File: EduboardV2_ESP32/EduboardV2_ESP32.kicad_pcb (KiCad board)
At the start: 2 copper layers, 2 parts, among them U1 ESP32-WROOM-E, U2 FT2232HL

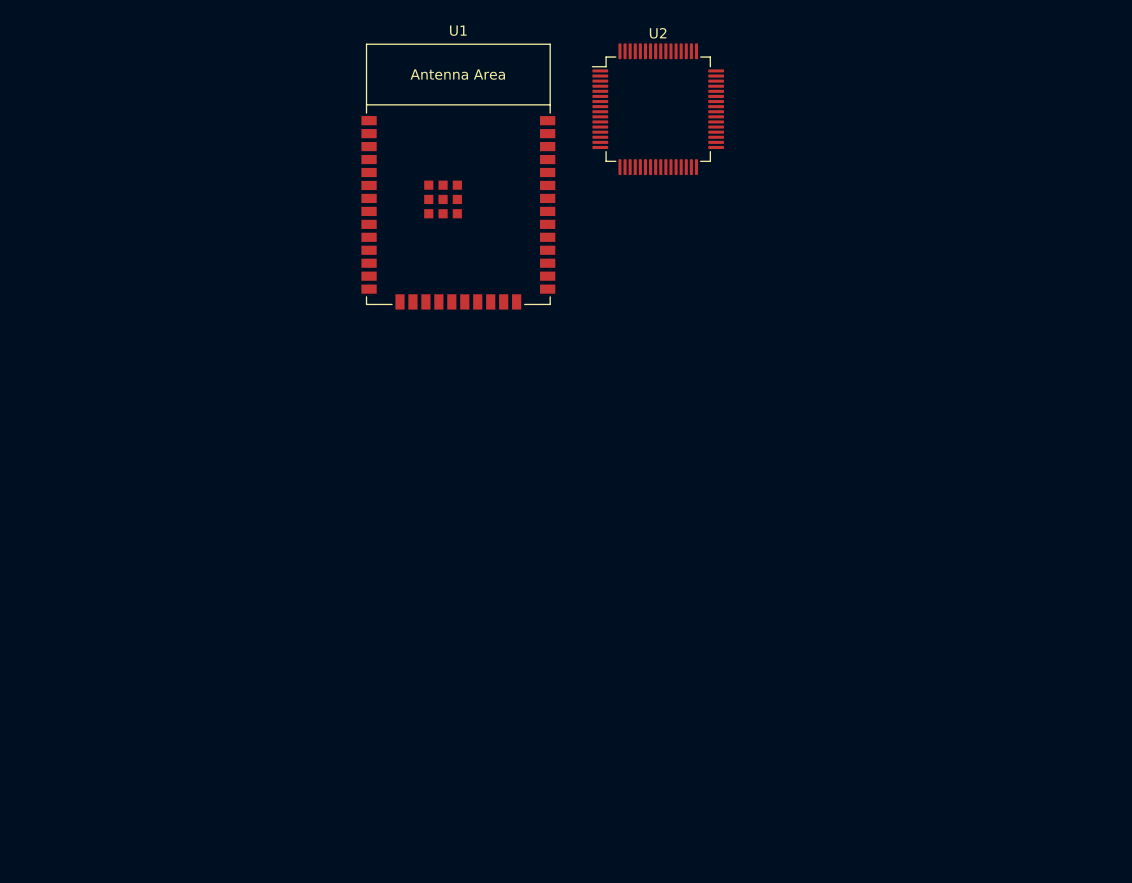
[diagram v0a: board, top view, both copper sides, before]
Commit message: finalize ft2232 design, prepare esp pins, work on mpcie pinout
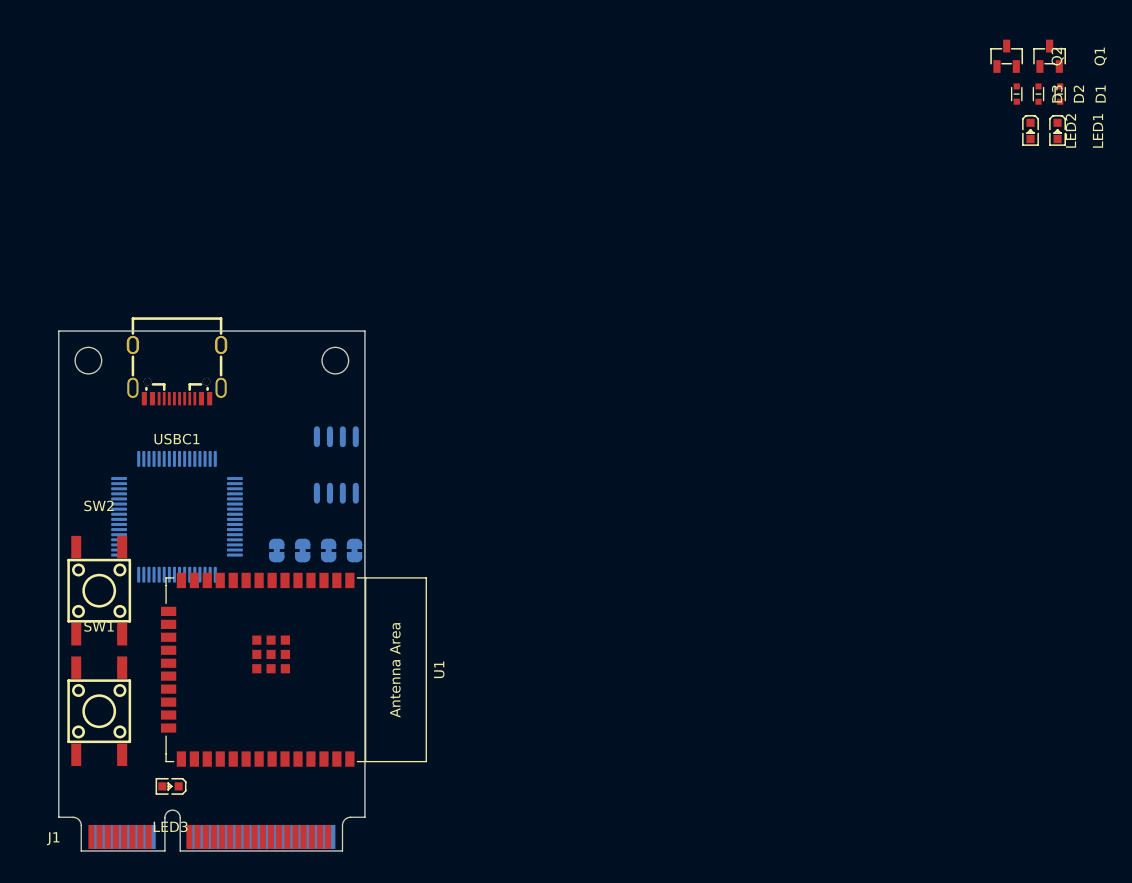
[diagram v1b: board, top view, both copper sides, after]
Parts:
- added D1: LESD5D5.0CT1G, JLCPCB:SOD-523_L1.2-W0.8-LS1.6-BI, F.Cu at (202.4, 82.1)
- added D2: LESD5D5.0CT1G, JLCPCB:SOD-523_L1.2-W0.8-LS1.6-BI, F.Cu at (200.2, 82.1)
- added D3: LESD5D5.0CT1G, JLCPCB:SOD-523_L1.2-W0.8-LS1.6-BI, F.Cu at (198.1, 82.1)
- added J1: Conn_02x26_Odd_Even, mpcie:mini-PCIe_F1_Full, F.Cu at (115.4, 156.3)
- added JP1: SolderJumper_2_Bridged, Jumper:SolderJumper-2_P1.3mm_Bridged_RoundedPad1.0x1.5mm, B.Cu at (133.2, 126.9)
- added JP2: SolderJumper_2_Bridged, Jumper:SolderJumper-2_P1.3mm_Bridged_RoundedPad1.0x1.5mm, B.Cu at (130.7, 126.9)
- added JP3: SolderJumper_2_Bridged, Jumper:SolderJumper-2_P1.3mm_Bridged_RoundedPad1.0x1.5mm, B.Cu at (128.1, 126.9)
- added JP4: SolderJumper_2_Bridged, Jumper:SolderJumper-2_P1.3mm_Bridged_RoundedPad1.0x1.5mm, B.Cu at (125.6, 126.9)
- added LED1: 19-217/BHC-ZL1M2RY/3T, JLCPCB:LED0603-RD, F.Cu at (202.1, 85.8)
- added LED2: 19-217/BHC-ZL1M2RY/3T, JLCPCB:LED0603-RD, F.Cu at (199.5, 85.8)
- added LED3: 19-217/BHC-ZL1M2RY/3T, JLCPCB:LED0603-RD, F.Cu at (115.2, 150.0)
- added Q1: S8050_C139514, JLCPCB:SOT-23-3_L2.9-W1.3-P1.90-LS2.4-BR, F.Cu at (201.3, 78.4)
- added Q2: S8050_C139514, JLCPCB:SOT-23-3_L2.9-W1.3-P1.90-LS2.4-BR, F.Cu at (197.1, 78.4)
- added SW1: K2-1102SP-C4SC-04, JLCPCB:KEY-SMD_4P-L6.0-W6.0-P4.50-LS9.5-BL, F.Cu at (108.2, 142.6)
- added SW2: K2-1102SP-C4SC-04, JLCPCB:KEY-SMD_4P-L6.0-W6.0-P4.50-LS9.5-BL, F.Cu at (108.2, 130.8)
- added U3: M93C46-WMN6TP, JLCPCB:SOIC-8_L4.9-W3.9-P1.27-LS6.0-BL, B.Cu at (131.4, 118.5)
- added USBC1: USB3.1C16PFSMT, JLCPCB:USB-C-SMD_TYPE-C-USB-17, F.Cu at (115.8, 109.4)
- U2: moved to B.Cu
- moved U2 61.8 mm to (115.8, 123.6), turned to -90 degrees
- moved U1 50.0 mm to (125.8, 138.6), turned to -90 degrees
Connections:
- U1 pad 1: Net-(U1-GND-Pad1) -> GND
- U1 pad 13: unconnected-(U1-MTMS/GPIO14/ADC2_CH6-Pad13) -> ESP_TMS
- U1 pad 14: unconnected-(U1-MTDI/GPIO12/ADC2_CH5-Pad14) -> ESP_TDI
- U1 pad 15: Net-(U1-GND-Pad1) -> GND
- U1 pad 16: unconnected-(U1-MTCK/GPIO13/ADC2_CH4-Pad16) -> ESP_TCK
- U1 pad 2: unconnected-(U1-3V3-Pad2) -> +3V3
- U1 pad 23: unconnected-(U1-MTDO/GPIO15/ADC2_CH3-Pad23) -> ESP_TDO
- U1 pad 25: unconnected-(U1-GPIO0/BOOT/ADC2_CH1-Pad25) -> ESP_IO0
- U1 pad 3: unconnected-(U1-EN/CHIP_PU-Pad3) -> ESP_EN
- U1 pad 34: unconnected-(U1-U0RXD/GPIO3-Pad34) -> ESP_RXD
- U1 pad 35: unconnected-(U1-U0TXD/GPIO1-Pad35) -> ESP_TXD
- U1 pad 38: Net-(U1-GND-Pad1) -> GND
- U1 pad 39: unconnected-(U1-GND_THERMAL-Pad39) -> GND
- U2 pad 12: unconnected-(U2-VCORE-Pad12) -> +1V8
- U2 pad 14: unconnected-(U2-~{RESET}-Pad14) -> Net-(U2-~{RESET})
- U2 pad 16: unconnected-(U2-ADBUS0-Pad16) -> FT_TCK
- U2 pad 17: unconnected-(U2-ADBUS1-Pad17) -> FT_TDI
- U2 pad 18: unconnected-(U2-ADBUS2-Pad18) -> FT_TDO
- U2 pad 19: unconnected-(U2-ADBUS3-Pad19) -> FT_TMS
- U2 pad 20: unconnected-(U2-VCCIO-Pad20) -> +3V3
- U2 pad 31: unconnected-(U2-VCCIO-Pad31) -> +3V3
- U2 pad 36: unconnected-(U2-~{SUSPEND}-Pad36) -> nSUSPEND
- U2 pad 37: unconnected-(U2-VCORE-Pad37) -> +1V8
- U2 pad 38: unconnected-(U2-BDBUS0-Pad38) -> FT_TXD
- U2 pad 39: unconnected-(U2-BDBUS1-Pad39) -> FT_RXD
- U2 pad 4: unconnected-(U2-VPHY-Pad4) -> Net-(U2-VPHY)
- U2 pad 40: unconnected-(U2-BDBUS2-Pad40) -> FT_nRTS
- U2 pad 42: unconnected-(U2-VCCIO-Pad42) -> +3V3
- U2 pad 43: unconnected-(U2-BDBUS4-Pad43) -> FT_nDTR
- U2 pad 49: unconnected-(U2-VREGOUT-Pad49) -> +1V8
- U2 pad 50: unconnected-(U2-VREGIN-Pad50) -> +3V3
- U2 pad 54: unconnected-(U2-BCBUS3-Pad54) -> Net-(LED1-C)
- U2 pad 55: unconnected-(U2-BCBUS4-Pad55) -> Net-(LED2-C)
- U2 pad 56: unconnected-(U2-VCCIO-Pad56) -> +3V3
- U2 pad 59: unconnected-(U2-BCBUS7-Pad59) -> nPWRSAV
- U2 pad 6: unconnected-(U2-REF-Pad6) -> Net-(U2-REF)
- U2 pad 60: unconnected-(U2-~{PWREN}-Pad60) -> nPWREN
- U2 pad 61: unconnected-(U2-EEDATA-Pad61) -> Net-(U2-EEDATA)
- U2 pad 62: unconnected-(U2-EECLK-Pad62) -> Net-(U2-EECLK)
- U2 pad 63: unconnected-(U2-EECS-Pad63) -> Net-(U2-EECS)
- U2 pad 64: unconnected-(U2-VCORE-Pad64) -> +1V8
- U2 pad 7: unconnected-(U2-DM-Pad7) -> D-
- U2 pad 8: unconnected-(U2-DP-Pad8) -> D+
- U2 pad 9: unconnected-(U2-VPLL-Pad9) -> Net-(U2-VPLL)
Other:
- board outline added: 30 x 51 mm

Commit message: all parts placed. descision about usb-debug line to be made...
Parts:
- added C1: 12p, Capacitor_SMD:C_0603_1608Metric, B.Cu at (109.7, 113.5)
- added C10: 100n, Capacitor_SMD:C_0603_1608Metric, F.Cu at (117.1, 120.8)
- added C11: 100n, Capacitor_SMD:C_0603_1608Metric, F.Cu at (112.3, 121.5)
- added C12: 100n, Capacitor_SMD:C_0603_1608Metric, B.Cu at (107.7, 126.2)
- added C13: 100n, Capacitor_SMD:C_0603_1608Metric, F.Cu at (112.6, 126.0)
- added C14: 100n, Capacitor_SMD:C_0603_1608Metric, F.Cu at (121.7, 122.8)
- added C15: 100n, Capacitor_SMD:C_0603_1608Metric, F.Cu at (121.7, 125.9)
- added C16: 100n, Capacitor_SMD:C_0603_1608Metric, F.Cu at (115.8, 127.5)
- added C17: 100n, Capacitor_SMD:C_0603_1608Metric, F.Cu at (128.5, 126.7)
- added C18: 100n, Capacitor_SMD:C_0603_1608Metric, B.Cu at (107.7, 136.4)
- added C19: 100n, Capacitor_SMD:C_0603_1608Metric, F.Cu at (132.3, 127.5)
- added C2: 12p, Capacitor_SMD:C_0603_1608Metric, B.Cu at (109.7, 117.1)
- added C20: 1u, Capacitor_SMD:C_0603_1608Metric, F.Cu at (132.3, 125.9)
- added C21: 1u, Capacitor_SMD:C_0603_1608Metric, B.Cu at (122.2, 143.0)
- added C22: 100n, Capacitor_SMD:C_0603_1608Metric, B.Cu at (122.2, 144.5)
- added C23: 100n, Capacitor_SMD:C_0603_1608Metric, B.Cu at (117.9, 148.7)
- added C24: 100n, Capacitor_SMD:C_0603_1608Metric, B.Cu at (126.5, 147.3)
- added C3: 100n, Capacitor_SMD:C_0603_1608Metric, B.Cu at (127.5, 121.8)
- added C4: 4u7, Capacitor_SMD:C_0805_2012Metric, B.Cu at (118.5, 131.4)
- added C5: 4u7, Capacitor_SMD:C_0805_2012Metric, B.Cu at (114.2, 131.3)
- added C6: 4u7, Capacitor_SMD:C_0805_2012Metric, B.Cu at (114.4, 114.3)
- added C7: 4u7, Capacitor_SMD:C_0805_2012Metric, B.Cu at (118.1, 114.3)
- added C8: 100n, Capacitor_SMD:C_0603_1608Metric, B.Cu at (117.9, 116.1)
- added C9: 100n, Capacitor_SMD:C_0603_1608Metric, B.Cu at (114.4, 116.1)
- added FB1: FerriteBead_Small, Inductor_SMD:L_0805_2012Metric, B.Cu at (117.2, 111.5)
- added FB2: FerriteBead_Small, Inductor_SMD:L_0805_2012Metric, B.Cu at (113.5, 111.5)
- added JP5: SolderJumper_2_Open, Jumper:SolderJumper-2_P1.3mm_Open_RoundedPad1.0x1.5mm, B.Cu at (121.5, 152.3)
- added JP6: SolderJumper_2_Open, Jumper:SolderJumper-2_P1.3mm_Open_RoundedPad1.0x1.5mm, B.Cu at (122.8, 141.0)
- added JP7: SolderJumper_3_Bridged12, Jumper:SolderJumper-3_P1.3mm_Bridged12_RoundedPad1.0x1.5mm, F.Cu at (111.4, 150.5)
- added JP8: SolderJumper_3_Bridged12, Jumper:SolderJumper-3_P1.3mm_Bridged12_RoundedPad1.0x1.5mm, F.Cu at (106.7, 150.5)
- added R1: 2k2, Resistor_SMD:R_0603_1608Metric, B.Cu at (132.6, 113.8)
- added R10: 33R, Resistor_SMD:R_0603_1608Metric, B.Cu at (123.8, 116.5)
- added R11: 33R, Resistor_SMD:R_0603_1608Metric, B.Cu at (123.8, 114.9)
- added R12: 33R, Resistor_SMD:R_0603_1608Metric, B.Cu at (123.8, 113.4)
- added R13: 2k2, Resistor_SMD:R_0603_1608Metric, F.Cu at (107.2, 117.5)
- added R14: 2k2, Resistor_SMD:R_0603_1608Metric, F.Cu at (105.5, 117.5)
- added R15: 0R, Resistor_SMD:R_0603_1608Metric, B.Cu at (129.3, 144.3)
- added R16: 0R, Resistor_SMD:R_0603_1608Metric, B.Cu at (127.7, 144.3)
- added R17: 10k, Resistor_SMD:R_0603_1608Metric, B.Cu at (113.4, 136.3)
- added R18: 10k, Resistor_SMD:R_0603_1608Metric, B.Cu at (118.9, 138.6)
- added R19: 10k, Resistor_SMD:R_0603_1608Metric, F.Cu at (130.0, 126.7)
- added R2: 10k, Resistor_SMD:R_0603_1608Metric, B.Cu at (126.9, 114.2)
- added R20: 10k, Resistor_SMD:R_0603_1608Metric, B.Cu at (107.7, 137.9)
- added R21: 0R, Resistor_SMD:R_0603_1608Metric, B.Cu at (131.7, 123.2)
- added R22: 2k2, Resistor_SMD:R_0603_1608Metric, B.Cu at (108.6, 140.2)
- added R23: 10k, Resistor_SMD:R_0603_1608Metric, B.Cu at (124.7, 151.8)
- added R24: 10k, Resistor_SMD:R_0603_1608Metric, B.Cu at (119.6, 141.0)
- added R3: 10k, Resistor_SMD:R_0603_1608Metric, B.Cu at (126.9, 112.6)
- added R4: 10k, Resistor_SMD:R_0603_1608Metric, B.Cu at (126.9, 115.7)
- added R5: 0R, Resistor_SMD:R_0603_1608Metric, B.Cu at (128.7, 124.5)
- added R6: 10k, Resistor_SMD:R_0603_1608Metric, F.Cu at (114.8, 115.1)
- added R7: 10k, Resistor_SMD:R_0603_1608Metric, F.Cu at (118.5, 115.1)
- added R8: 1k, Resistor_SMD:R_0603_1608Metric, F.Cu at (118.6, 120.8)
- added R9: 12k, Resistor_SMD:R_0603_1608Metric, F.Cu at (114.6, 120.8)
- added U4: SX1509BIULTRT, EduboardV2_kicadlib:QFN-28_L4.0-W4.0-P0.40-BL-EP, B.Cu at (122.6, 148.0)
- added Y2: 12MHz, Crystal:Crystal_SMD_3225-4Pin_3.2x2.5mm, B.Cu at (106.8, 115.2)
- J1: value Conn_02x26_Odd_Even -> EduboardV2 PCIE UP Board Connector; footprint mpcie:mini-PCIe_F1_Full -> EduboardV2_kicadlib:mini-PCIe_F1_Full
- Q1, Q2: moved to B.Cu
- moved LED1 101.1 mm to (107.2, 120.5), turned to 90 degrees
- moved LED2 100.2 mm to (105.5, 120.5), turned to 90 degrees
- moved Q1 100.0 mm to (119.8, 136.3), turned to 180 degrees
- moved Q2 99.4 mm to (116.3, 136.3), turned to 180 degrees
- moved D1 95.3 mm to (112.5, 113.8), turned to 0 degrees
- moved D3 88.9 mm to (115.1, 113.8), turned to 0 degrees
- moved D2 88.5 mm to (117.6, 113.8), turned to 180 degrees
- moved J1 1.14 mm to (115.5, 157.4)
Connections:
- J1 pad 1: unconnected-(J1-Pin_1-Pad1) -> GND
- J1 pad 10: unconnected-(J1-Pin_10-Pad10) -> USB_Debug_D-
- J1 pad 11: unconnected-(J1-Pin_11-Pad11) -> Net-(J1-UART0_UP_RX)
- J1 pad 12: unconnected-(J1-Pin_12-Pad12) -> USB_Debug_D+
- J1 pad 13: unconnected-(J1-Pin_13-Pad13) -> Net-(J1-UART1_RS485_TX)
- J1 pad 14: unconnected-(J1-Pin_14-Pad14) -> GND
- J1 pad 15: unconnected-(J1-Pin_15-Pad15) -> Net-(J1-UART1_RS485_RX)
- J1 pad 16: unconnected-(J1-Pin_16-Pad16) -> GPIO_RS485_DE
- J1 pad 17: unconnected-(J1-Pin_17-Pad17) -> ESP_TMS
- J1 pad 18: unconnected-(J1-Pin_18-Pad18) -> ESP_IO4
- J1 pad 19: unconnected-(J1-Pin_19-Pad19) -> ESP_TDI
- J1 pad 2: unconnected-(J1-Pin_2-Pad2) -> VBUS
- J1 pad 20: unconnected-(J1-Pin_20-Pad20) -> ESP_IO5
- J1 pad 21: unconnected-(J1-Pin_21-Pad21) -> ESP_TCK
- J1 pad 22: unconnected-(J1-Pin_22-Pad22) -> ESP_IO2
- J1 pad 23: unconnected-(J1-Pin_23-Pad23) -> ESP_TDO
- J1 pad 24: unconnected-(J1-Pin_24-Pad24) -> ESP_IO18
- J1 pad 25: unconnected-(J1-Pin_25-Pad25) -> GPIO_RotEnc_SW
- J1 pad 26: unconnected-(J1-Pin_26-Pad26) -> ESP_IO19
- J1 pad 27: unconnected-(J1-Pin_27-Pad27) -> ESP_IO33
- J1 pad 28: unconnected-(J1-Pin_28-Pad28) -> ESP_IO23
- J1 pad 29: unconnected-(J1-Pin_29-Pad29) -> ESP_IO27
- J1 pad 3: unconnected-(J1-Pin_3-Pad3) -> +5V
- J1 pad 30: unconnected-(J1-Pin_30-Pad30) -> ESP_IO22
- J1 pad 31: unconnected-(J1-Pin_31-Pad31) -> GPIO_PWM_R
- J1 pad 32: unconnected-(J1-Pin_32-Pad32) -> ESP_IO21
- J1 pad 33: unconnected-(J1-Pin_33-Pad33) -> GPIO_PWM_G
- J1 pad 34: unconnected-(J1-Pin_34-Pad34) -> ESP_IO0
- J1 pad 35: unconnected-(J1-Pin_35-Pad35) -> GPIO_PWM_B
- J1 pad 36: unconnected-(J1-Pin_36-Pad36) -> ESP_IO32
- J1 pad 37: unconnected-(J1-Pin_37-Pad37) -> GPIO_LED0
- J1 pad 38: unconnected-(J1-Pin_38-Pad38) -> ESP_IO25
- J1 pad 39: unconnected-(J1-Pin_39-Pad39) -> GPIO_LED1
- J1 pad 4: unconnected-(J1-Pin_4-Pad4) -> +5V
- J1 pad 40: unconnected-(J1-Pin_40-Pad40) -> ESP_IO35
- J1 pad 41: unconnected-(J1-Pin_41-Pad41) -> GPIO_LED2
- J1 pad 42: unconnected-(J1-Pin_42-Pad42) -> ESP_IO26
- J1 pad 43: unconnected-(J1-Pin_43-Pad43) -> GPIO_LED3
- J1 pad 44: unconnected-(J1-Pin_44-Pad44) -> ESP_IO36
- J1 pad 45: unconnected-(J1-Pin_45-Pad45) -> GPIO_LED4
- J1 pad 46: unconnected-(J1-Pin_46-Pad46) -> ESP_IO34
- J1 pad 47: unconnected-(J1-Pin_47-Pad47) -> GPIO_LED5
- J1 pad 48: unconnected-(J1-Pin_48-Pad48) -> ESP_IO39
- J1 pad 49: unconnected-(J1-Pin_49-Pad49) -> GPIO_LED6
- J1 pad 5: unconnected-(J1-Pin_5-Pad5) -> +3V3
- J1 pad 50: unconnected-(J1-Pin_50-Pad50) -> GPIO_SW2
- J1 pad 51: unconnected-(J1-Pin_51-Pad51) -> GPIO_LED7
- J1 pad 52: unconnected-(J1-Pin_52-Pad52) -> GPIO_SW3
- J1 pad 6: unconnected-(J1-Pin_6-Pad6) -> +3V3
- J1 pad 7: unconnected-(J1-Pin_7-Pad7) -> GND
- J1 pad 8: unconnected-(J1-Pin_8-Pad8) -> GND
- J1 pad 9: unconnected-(J1-Pin_9-Pad9) -> Net-(J1-UART0_UP_TX)
- U1 pad 10: unconnected-(U1-DAC_1/ADC2_CH8/GPIO25-Pad10) -> ESP_IO25
- U1 pad 11: unconnected-(U1-DAC_2/ADC2_CH9/GPIO26-Pad11) -> ESP_IO26
- U1 pad 12: unconnected-(U1-ADC2_CH7/GPIO27-Pad12) -> ESP_IO27
- U1 pad 24: unconnected-(U1-ADC2_CH2/GPIO2-Pad24) -> ESP_IO2
- U1 pad 26: unconnected-(U1-ADC2_CH0/GPIO4-Pad26) -> ESP_IO4
- U1 pad 27: unconnected-(U1-GPIO16-Pad27) -> ESP_IO16
- U1 pad 28: unconnected-(U1-GPIO17-Pad28) -> ESP_IO17
- U1 pad 29: unconnected-(U1-GPIO5-Pad29) -> ESP_IO5
- U1 pad 30: unconnected-(U1-GPIO18-Pad30) -> ESP_IO18
- U1 pad 31: unconnected-(U1-GPIO19-Pad31) -> ESP_IO19
- U1 pad 33: unconnected-(U1-GPIO21-Pad33) -> ESP_IO21
- U1 pad 36: unconnected-(U1-GPIO22-Pad36) -> ESP_IO22
- U1 pad 37: unconnected-(U1-GPIO23-Pad37) -> ESP_IO23
- U1 pad 4: unconnected-(U1-SENSOR_VP/GPIO36/ADC1_CH0-Pad4) -> ESP_IO36
- U1 pad 5: unconnected-(U1-SENSOR_VN/GPIO39/ADC1_CH3-Pad5) -> ESP_IO39
- U1 pad 6: unconnected-(U1-GPIO34/ADC1_CH6-Pad6) -> ESP_IO34
- U1 pad 7: unconnected-(U1-GPIO35/ADC1_CH7-Pad7) -> ESP_IO35
- U1 pad 8: unconnected-(U1-32K_XP/GPIO32/ADC1_CH4-Pad8) -> ESP_IO32
- U1 pad 9: unconnected-(U1-32K_XN/GPIO33/ADC1_CH5-Pad9) -> ESP_IO33
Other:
- board size 30 x 51 mm -> 30 x 50.9 mm

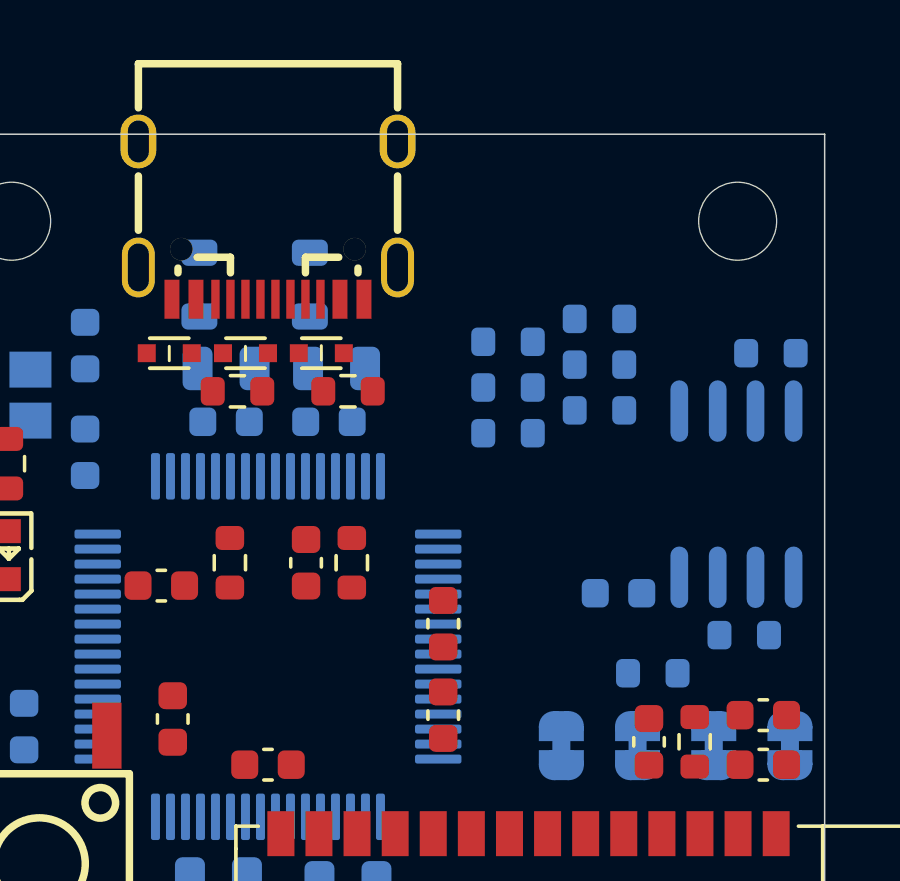
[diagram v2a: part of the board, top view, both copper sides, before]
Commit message: add voltage selector to prevent fighting sources
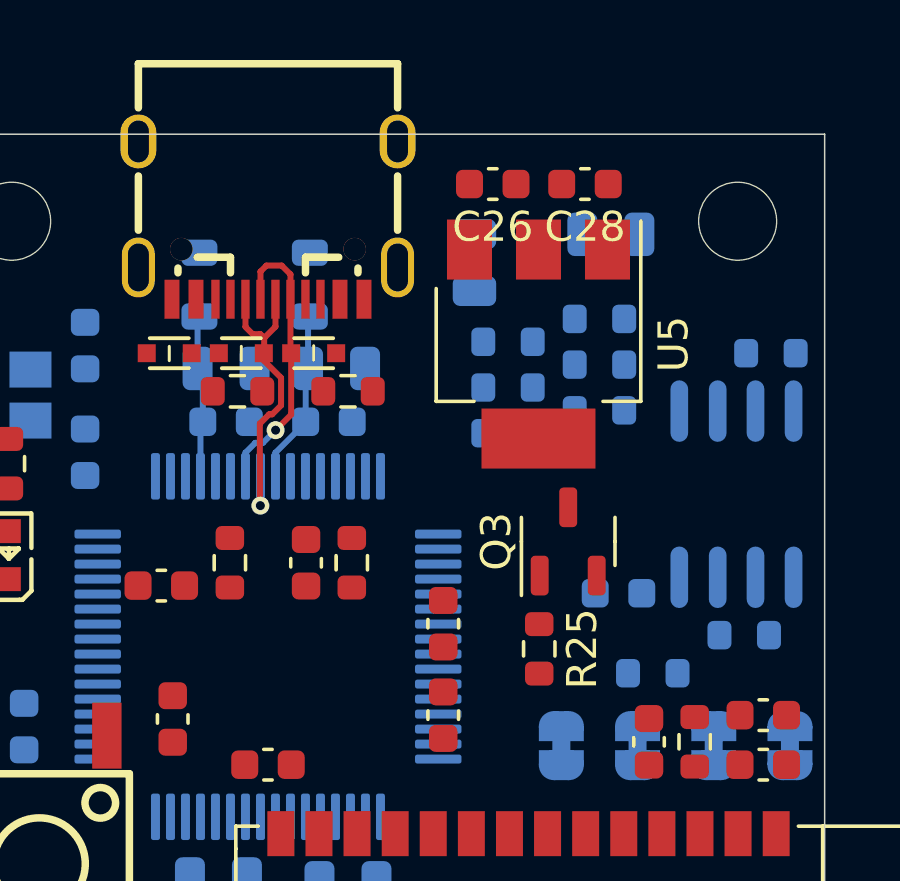
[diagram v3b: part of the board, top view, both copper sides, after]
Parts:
- added C25: 4u7, Capacitor_SMD:C_0805_2012Metric, B.Cu at (122.7, 110.8)
- added C26: 100n, Capacitor_SMD:C_0603_1608Metric, F.Cu at (123.3, 108.2)
- added C27: 4u7, Capacitor_SMD:C_0805_2012Metric, B.Cu at (127.3, 109.8)
- added C28: 100n, Capacitor_SMD:C_0603_1608Metric, F.Cu at (126.4, 108.2)
- added Q3: AO3401A, Package_TO_SOT_SMD:SOT-23-3, F.Cu at (125.8, 120.1)
- added R25: 2k2, Resistor_SMD:R_0603_1608Metric, F.Cu at (124.9, 123.6)
- added U5: LD1117S33TR_SOT223, Package_TO_SOT_SMD:SOT-223-3_TabPin2, F.Cu at (124.8, 113.5)
- moved D2 2.67 mm to (114.9, 113.8), turned to 0 degrees
- moved D3 2.27 mm to (117.3, 113.8), turned to 180 degrees
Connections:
- J1 pad 6: +3V3 -> 3.3V_Sense
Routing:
- net D+: track 0.00 -> 10.3 mm, vias 0 -> 1
- net D-: track 0.00 -> 9.65 mm, vias 0 -> 1
- net Net-(U2-VPLL): track 0.00 -> 5.80 mm
- net Net-(U2-VPHY): track 0.00 -> 5.46 mm
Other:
- copper layers 2 -> 4
